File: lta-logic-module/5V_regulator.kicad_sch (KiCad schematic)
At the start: 6 parts, among them U2 LM2595T-5

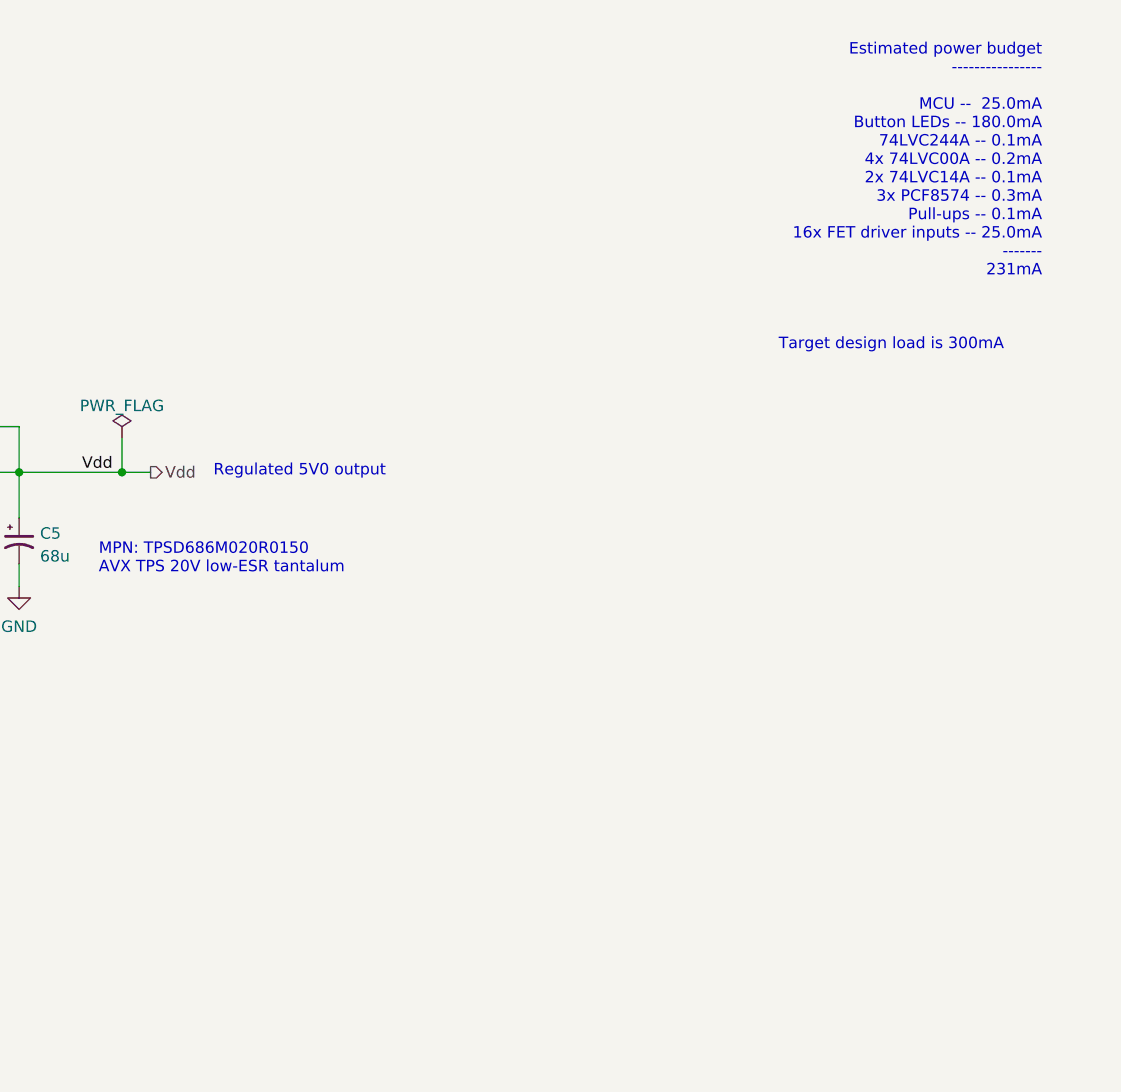
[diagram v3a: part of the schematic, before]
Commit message: Initial PCB setup
* Configure Elecrow DRC checks for lta-logic-module.
* Switch SN74LVC244A from 'N' PDIP to 'DWR' SOIC footprint.
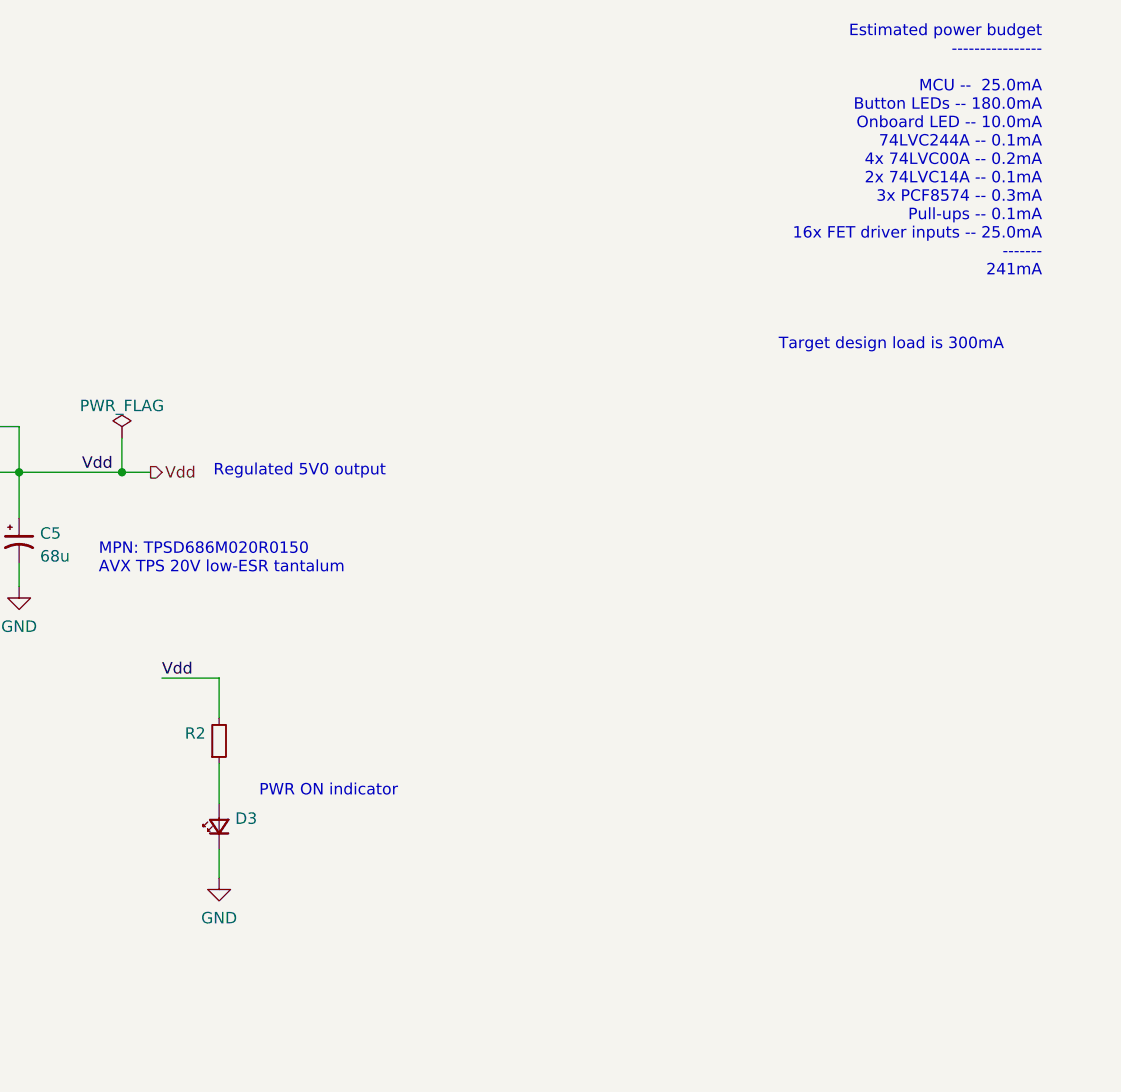
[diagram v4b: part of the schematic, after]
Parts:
- added D3: (no value), symbol Device:LED_Small
- added R2: (no value), Resistor_SMD:R_0603_1608Metric, symbol Device:R_Small
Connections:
- net GND: now also D3.1 (K)
- net Vdd: now also R2.2
- new net: D3.2 (A), R2.1
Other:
- note added: "Estimated power budget ---------------- MCU -- 25.0mA Button LEDs -- 180.0mA Onboard LED -- 10.0mA 74LVC244A -- 0.1mA 4x 74LVC00A -- 0.2mA 2x 74LVC14A -- 0.1mA 3x PCF8574 -- 0.3mA Pull-ups -- 0.1mA 16x FET driver inputs -- 25.0mA ------- 241mA"
- note added: "PWR ON indicator"
- note removed: "Estimated power budget ---------------- MCU -- 25.0mA Button LEDs -- 180.0mA 74LVC244A -- 0.1mA 4x 74LVC00A -- 0.2mA 2x 74LVC14A -- 0.1mA 3x PCF8574 -- 0.3mA Pull-ups -- 0.1mA 16x FET driver inputs -- 25.0mA ------- 231mA"
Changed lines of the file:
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@@
+    (stroke (width 0) (type default) (color 0 0 0 0))
+  )
+  (wire (pts (xy 176.53 92.71) (xy 176.53 97.155))
     (stroke (width 0) (type default) (color 0 0 0 0))
   )
@@
     (stroke (width 0) (type default) (color 0 0 0 0))
   )
+  (wire (pts (xy 176.53 102.235) (xy 176.53 106.68))
+    (stroke (width 0) (type default) (color 0 0 0 0))
+  )
   (wire (pts (xy 107.315 69.85) (xy 107.315 71.12))
     (stroke (width 0) (type default) (color 0 0 0 0))
@@
     (stroke (width 0) (type default) (color 0 0 0 0))
   )
+  (wire (pts (xy 176.53 111.76) (xy 176.53 114.935))
+    (stroke (width 0) (type default) (color 0 0 0 0))
+  )
   (wire (pts (xy 107.315 76.835) (xy 121.92 76.835))
     (stroke (width 0) (type default) (color 0 0 0 0))
@@
   )
   (wire (pts (xy 96.52 76.835) (xy 107.315 76.835))
+    (stroke (width 0) (type default) (color 0 0 0 0))
+  )
+  (wire (pts (xy 170.18 92.71) (xy 176.53 92.71))
     (stroke (width 0) (type default) (color 0 0 0 0))
   )
@@
     (effects (font (size 1.27 1.27)) (justify left bottom))
   )
+  (text "PWR ON indicator" (at 180.975 106.045 0)
+    (effects (font (size 1.27 1.27)) (justify left bottom))
+  )
   (text "8--28Vin, 24V typ" (at 71.12 61.595 0)
     (effects (font (size 1.27 1.27)) (justify left bottom))
@@
     (effects (font (size 1.27 1.27)) (justify left bottom))
   )
-  (text "Estimated power budget\n----------------\n\nMCU --  25.0mA\nButton LEDs -- 180.0mA\n74LVC244A -- 0.1mA\n4x 74LVC00A -- 0.2mA\n2x 74LVC14A -- 0.1mA\n3x PCF8574 -- 0.3mA\nPull-ups -- 0.1mA\n16x FET driver inputs -- 25.0mA\n-------\n231mA"
+  (text "Estimated power budget\n----------------\n\nMCU --  25.0mA\nButton LEDs -- 180.0mA\nOnboard LED -- 10.0mA\n74LVC244A -- 0.1mA\n4x 74LVC00A -- 0.2mA\n2x 74LVC14A -- 0.1mA\n3x PCF8574 -- 0.3mA\nPull-ups -- 0.1mA\n16x FET driver inputs -- 25.0mA\n-------\n241mA"
     (at 267.97 48.26 0)
     (effects (font (size 1.27 1.27)) (justify right bottom))
@@
   )
   (label "VBATT" (at 89.535 64.77 0)
+    (effects (font (size 1.27 1.27)) (justify left bottom))
+  )
+  (label "Vdd" (at 170.18 92.71 0)
     (effects (font (size 1.27 1.27)) (justify left bottom))
   )
@@
     (pin "2")
   )
+  (symbol (lib_id "Device:R_Small") (at 176.53 99.695 0) (mirror x) (unit 1)
+    (in_bom yes) (on_board yes) (fields_autoplaced)
+    (property "Reference" "R2" (id 0) (at 175.0314 98.8603 0)
+      (effects (font (size 1.27 1.27)) (justify right))
+    )
+    (property "Value" "" (id 1) (at 175.0314 101.3972 0)
+      (effects (font (size 1.27 1.27)) (justify right))
+    )
+    (property "Footprint" "Resistor_SMD:R_0603_1608Metric" (id 2) (at 176.53 99.695 0)
+      (effects (font (size 1.27 1.27)) hide)
+    )
+    (property "Datasheet" "~" (id 3) (at 176.53 99.695 0)
+      (effects (font (size 1.27 1.27)) hide)
+    )
+    (property "Comment" "10K 0603 resistor; +/-1%; 1/10W " (id 4) (at 176.53 99.695 0)
+      (effects (font (size 1.27 1.27)) hide)
+    )
+    (property "MANUFACTURER" "YAEGO" (id 5) (at 176.53 99.695 0)
+      (effects (font (size 1.27 1.27)) hide)
+    )
+    (property "MPN" "RC0603FR-0710KL" (id 6) (at 176.53 99.695 0)
+      (effects (font (size 1.27 1.27)) hide)
+    )
+    (pin "1")
+    (pin "2")
+  )
   (symbol (lib_id "power:GND") (at 139.7 82.55 0) (unit 1)
     (in_bom yes) (on_board yes) (fields_autoplaced)
@@
     )
     (property "Datasheet" "" (id 3) (at 28.575 36.83 0)
+      (effects (font (size 1.27 1.27)) hide)
+    )
+    (pin "1")
+  )
+  (symbol (lib_id "power:GND") (at 176.53 114.935 0) (unit 1)
+    (in_bom yes) (on_board yes) (fields_autoplaced)
+    (property "Reference" "#PWR021" (id 0) (at 176.53 121.285 0)
+      (effects (font (size 1.27 1.27)) hide)
+    )
+    (property "Value" "GND" (id 1) (at 176.53 119.3784 0))
+    (property "Footprint" "" (id 2) (at 176.53 114.935 0)
+      (effects (font (size 1.27 1.27)) hide)
+    )
+    (property "Datasheet" "" (id 3) (at 176.53 114.935 0)
       (effects (font (size 1.27 1.27)) hide)
     )
@@
     (pin "1")
   )
+  (symbol (lib_id "Device:LED_Small") (at 176.53 109.22 90) (unit 1)
+    (in_bom yes) (on_board yes) (fields_autoplaced)
+    (property "Reference" "D3" (id 0) (at 178.308 108.3218 90)
+      (effects (font (size 1.27 1.27)) (justify right))
+    )
+    (property "Value" "" (id 1) (at 178.308 110.8587 90)
+      (effects (font (size 1.27 1.27)) (justify right))
+    )
+    (property "Footprint" "" (id 2) (at 176.53 109.22 90)
+      (effects (font (size 1.27 1.27)) hide)
+    )
+    (property "Datasheet" "https://media.digikey.com/pdf/Data%20Sheets/Harvatek%20PDFs/B1931URO-20D000114U1930.pdf" (id 3) (at 176.53 109.22 90)
+      (effects (font (size 1.27 1.27)) hide)
+    )
+    (property "MPN" "3147-B1931URO-20D000114U1930CT-ND" (id 4) (at 176.53 109.22 90)
+      (effects (font (size 1.27 1.27)) hide)
+    )
+    (property "MANUFACTURER" "Harvatek" (id 5) (at 176.53 109.22 90)
+      (effects (font (size 1.27 1.27)) hide)
+    )
+    (pin "1")
+    (pin "2")
+  )
 )

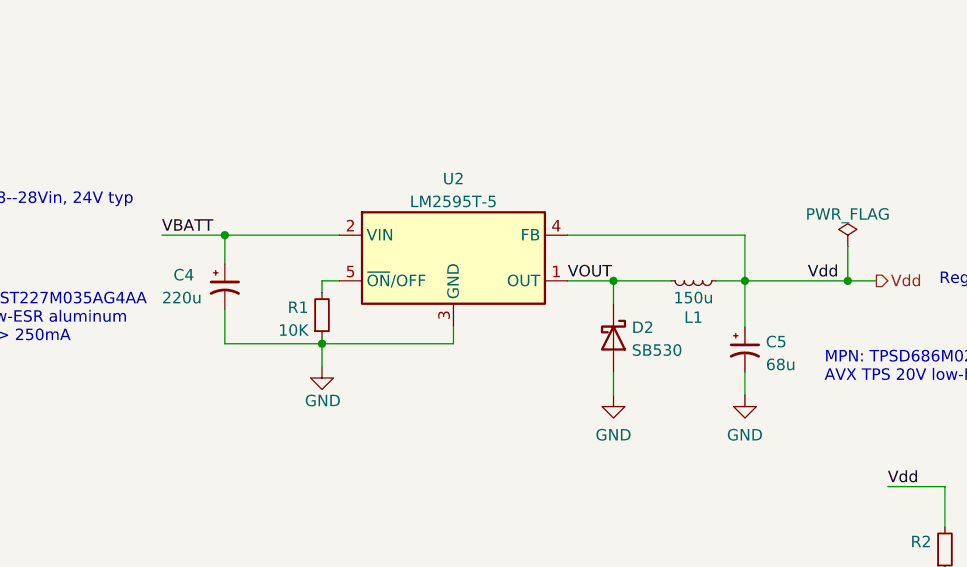
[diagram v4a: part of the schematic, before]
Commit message: Add light sensor circuit.
Adjust TODOs and comments after testing btn circuit.
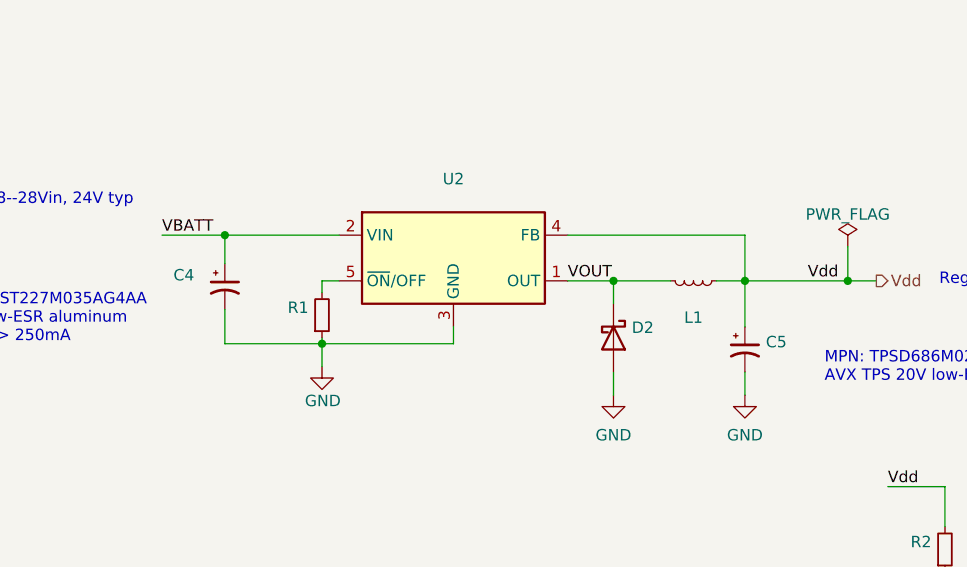
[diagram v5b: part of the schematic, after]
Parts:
- C4: value 220u -> (none); footprint Capacitor_THT:CP_Radial_D8.0mm_P3.50mm -> (none)
- C5: value 68u -> (none); footprint Capacitor_Tantalum_SMD:CP_EIA-7343-30_AVX-N -> (none)
- D2: value SB530 -> (none); footprint Diode_THT:D_DO-201AD_P15.24mm_Horizontal -> (none)
- D3: Comment (none) -> Vf=2.0V 20mA test current red LED
- L1: value 150u -> (none); footprint Aaron_THT:L_Radial_D13.5mm_P7.50mm -> (none)
- R1: value 10K -> (none); footprint Resistor_SMD:R_0603_1608Metric -> (none)
- R2: footprint Resistor_SMD:R_0603_1608Metric -> (none)
- U2: value LM2595T-5 -> (none); footprint Package_TO_SOT_THT:TO-220-5_P3.4x3.7mm_StaggerOdd_Lead3.8mm_Vertical -> (none)
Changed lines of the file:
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@@
   (symbol (lib_id "power:GND") (at 154.305 82.55 0) (unit 1)
     (in_bom yes) (on_board yes) (fields_autoplaced)
-    (property "Reference" "#PWR020" (id 0) (at 154.305 88.9 0)
+    (property "Reference" "#PWR022" (id 0) (at 154.305 88.9 0)
       (effects (font (size 1.27 1.27)) hide)
     )
@@
       (effects (font (size 1.27 1.27)) (justify left))
     )
-    (property "Value" "220u" (id 1) (at 89.535 71.755 0)
-      (effects (font (size 1.27 1.27)) (justify left))
-    )
-    (property "Footprint" "Capacitor_THT:CP_Radial_D8.0mm_P3.50mm" (id 2) (at 96.52 70.485 0)
+    (property "Value" "" (id 1) (at 89.535 71.755 0)
+      (effects (font (size 1.27 1.27)) (justify left))
+    )
+    (property "Footprint" "" (id 2) (at 96.52 70.485 0)
       (effects (font (size 1.27 1.27)) hide)
     )
@@
       (effects (font (size 1.27 1.27)) (justify right))
     )
-    (property "Value" "10K" (id 1) (at 105.8165 75.3622 0)
-      (effects (font (size 1.27 1.27)) (justify right))
-    )
-    (property "Footprint" "Resistor_SMD:R_0603_1608Metric" (id 2) (at 107.315 73.66 0)
+    (property "Value" "" (id 1) (at 105.8165 75.3622 0)
+      (effects (font (size 1.27 1.27)) (justify right))
+    )
+    (property "Footprint" "" (id 2) (at 107.315 73.66 0)
       (effects (font (size 1.27 1.27)) hide)
     )
@@
     (in_bom yes) (on_board yes)
     (property "Reference" "L1" (id 0) (at 148.59 73.9308 90))
-    (property "Value" "150u" (id 1) (at 148.59 71.755 90))
-    (property "Footprint" "Aaron_THT:L_Radial_D13.5mm_P7.50mm" (id 2) (at 148.59 69.85 0)
+    (property "Value" "" (id 1) (at 148.59 71.755 90))
+    (property "Footprint" "" (id 2) (at 148.59 69.85 0)
       (effects (font (size 1.27 1.27)) hide)
     )
@@
       (effects (font (size 1.27 1.27)) (justify left))
     )
-    (property "Value" "SB530" (id 1) (at 141.732 77.5847 90)
-      (effects (font (size 1.27 1.27)) (justify left))
-    )
-    (property "Footprint" "Diode_THT:D_DO-201AD_P15.24mm_Horizontal" (id 2) (at 139.7 76.2 0)
+    (property "Value" "" (id 1) (at 141.732 77.5847 90)
+      (effects (font (size 1.27 1.27)) (justify left))
+    )
+    (property "Footprint" "" (id 2) (at 139.7 76.2 0)
       (effects (font (size 1.27 1.27)) hide)
     )
@@
       (effects (font (size 1.27 1.27)) (justify right))
     )
-    (property "Footprint" "Resistor_SMD:R_0603_1608Metric" (id 2) (at 176.53 99.695 0)
+    (property "Footprint" "" (id 2) (at 176.53 99.695 0)
       (effects (font (size 1.27 1.27)) hide)
     )
@@
   (symbol (lib_id "power:GND") (at 139.7 82.55 0) (unit 1)
     (in_bom yes) (on_board yes) (fields_autoplaced)
-    (property "Reference" "#PWR019" (id 0) (at 139.7 88.9 0)
+    (property "Reference" "#PWR021" (id 0) (at 139.7 88.9 0)
       (effects (font (size 1.27 1.27)) hide)
     )
@@
   (symbol (lib_id "power:GND") (at 28.575 36.83 0) (unit 1)
     (in_bom yes) (on_board yes) (fields_autoplaced)
-    (property "Reference" "#PWR017" (id 0) (at 28.575 43.18 0)
+    (property "Reference" "#PWR019" (id 0) (at 28.575 43.18 0)
       (effects (font (size 1.27 1.27)) hide)
     )
@@
   (symbol (lib_id "power:GND") (at 176.53 114.935 0) (unit 1)
     (in_bom yes) (on_board yes) (fields_autoplaced)
-    (property "Reference" "#PWR021" (id 0) (at 176.53 121.285 0)
+    (property "Reference" "#PWR023" (id 0) (at 176.53 121.285 0)
       (effects (font (size 1.27 1.27)) hide)
     )
@@
   (symbol (lib_id "power:GND") (at 107.315 79.375 0) (unit 1)
     (in_bom yes) (on_board yes)
-    (property "Reference" "#PWR018" (id 0) (at 107.315 85.725 0)
+    (property "Reference" "#PWR020" (id 0) (at 107.315 85.725 0)
       (effects (font (size 1.27 1.27)) hide)
     )
@@
     (in_bom yes) (on_board yes) (fields_autoplaced)
     (property "Reference" "U2" (id 0) (at 121.92 58.5302 0))
-    (property "Value" "LM2595T-5" (id 1) (at 121.92 61.0671 0))
-    (property "Footprint" "Package_TO_SOT_THT:TO-220-5_P3.4x3.7mm_StaggerOdd_Lead3.8mm_Vertical" (id 2) (at 123.19 73.66 0)
+    (property "Value" "" (id 1) (at 121.92 61.0671 0))
+    (property "Footprint" "" (id 2) (at 123.19 73.66 0)
       (effects (font (size 1.27 1.27) italic) (justify left) hide)
     )
@@
       (effects (font (size 1.27 1.27)) (justify left))
     )
-    (property "Value" "68u" (id 1) (at 156.6291 79.1785 0)
-      (effects (font (size 1.27 1.27)) (justify left))
-    )
-    (property "Footprint" "Capacitor_Tantalum_SMD:CP_EIA-7343-30_AVX-N" (id 2) (at 154.305 77.47 0)
+    (property "Value" "" (id 1) (at 156.6291 79.1785 0)
+      (effects (font (size 1.27 1.27)) (justify left))
+    )
+    (property "Footprint" "" (id 2) (at 154.305 77.47 0)
       (effects (font (size 1.27 1.27)) hide)
     )
@@
       (effects (font (size 1.27 1.27)) hide)
     )
+    (property "Comment" "Vf=2.0V 20mA test current red LED" (id 6) (at 176.53 109.22 90)
+      (effects (font (size 1.27 1.27)) hide)
+    )
